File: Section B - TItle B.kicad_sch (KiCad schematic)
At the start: 0 parts

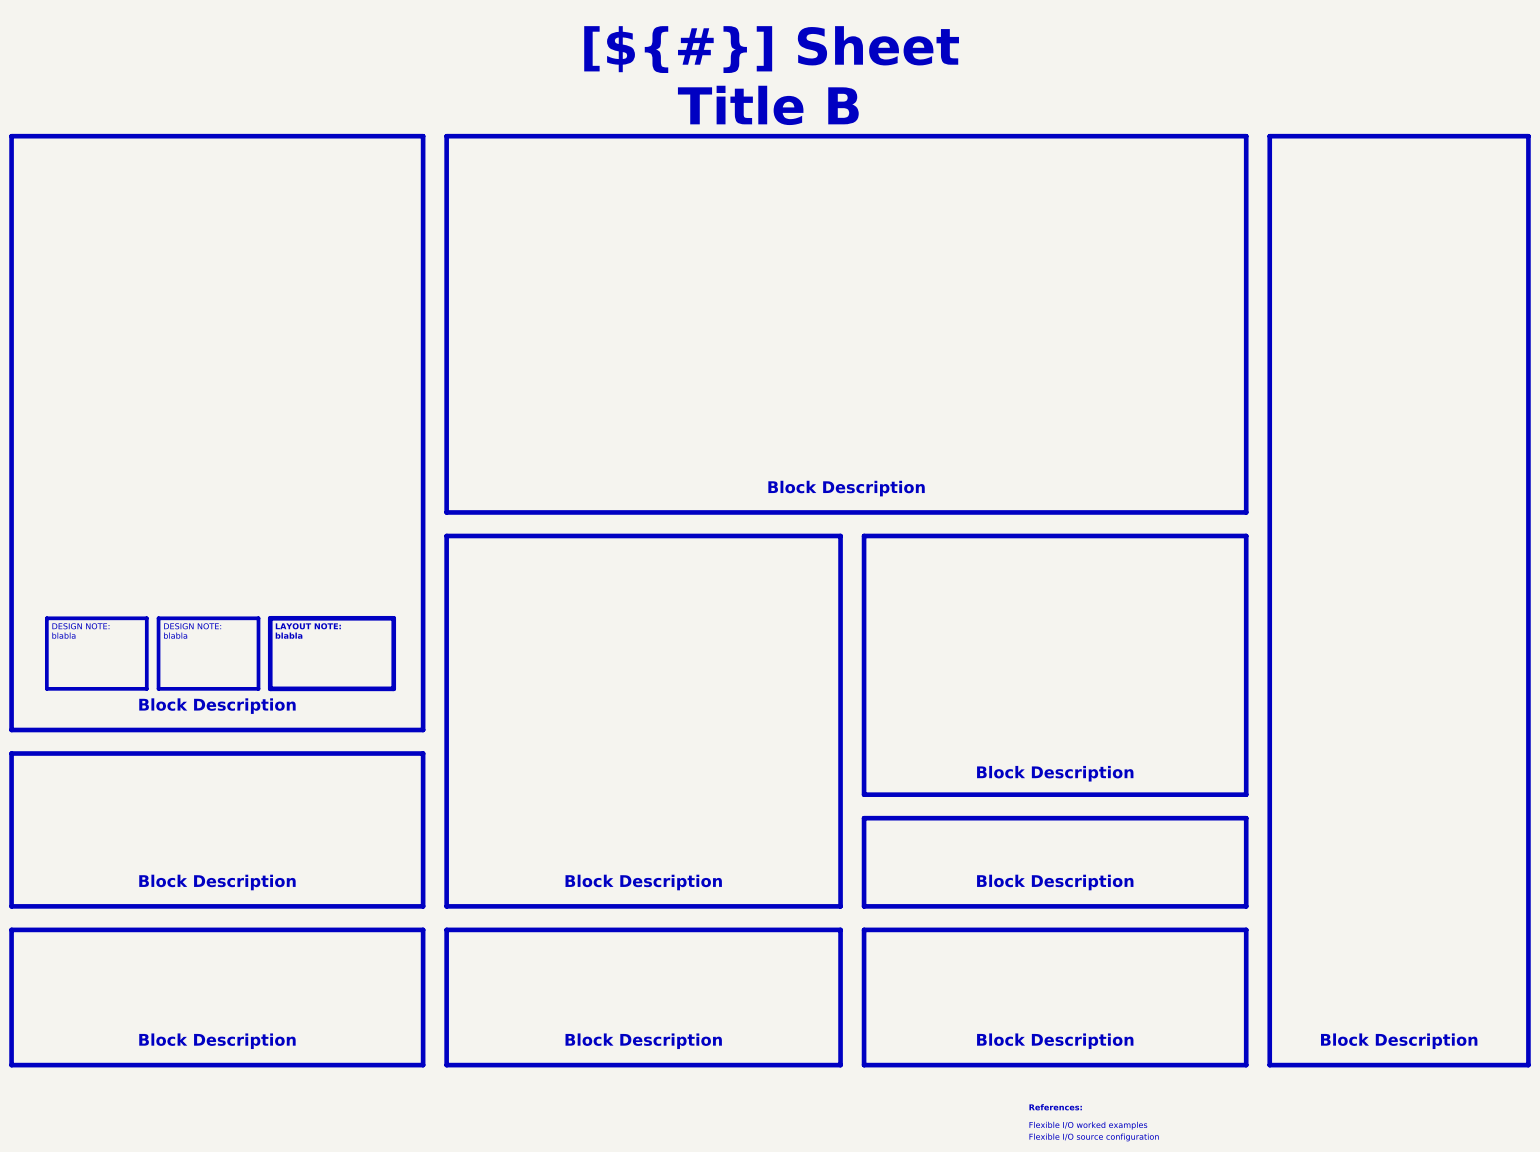
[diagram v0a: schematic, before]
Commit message: feat: Changed templates to be specific to Ryan Dynamics
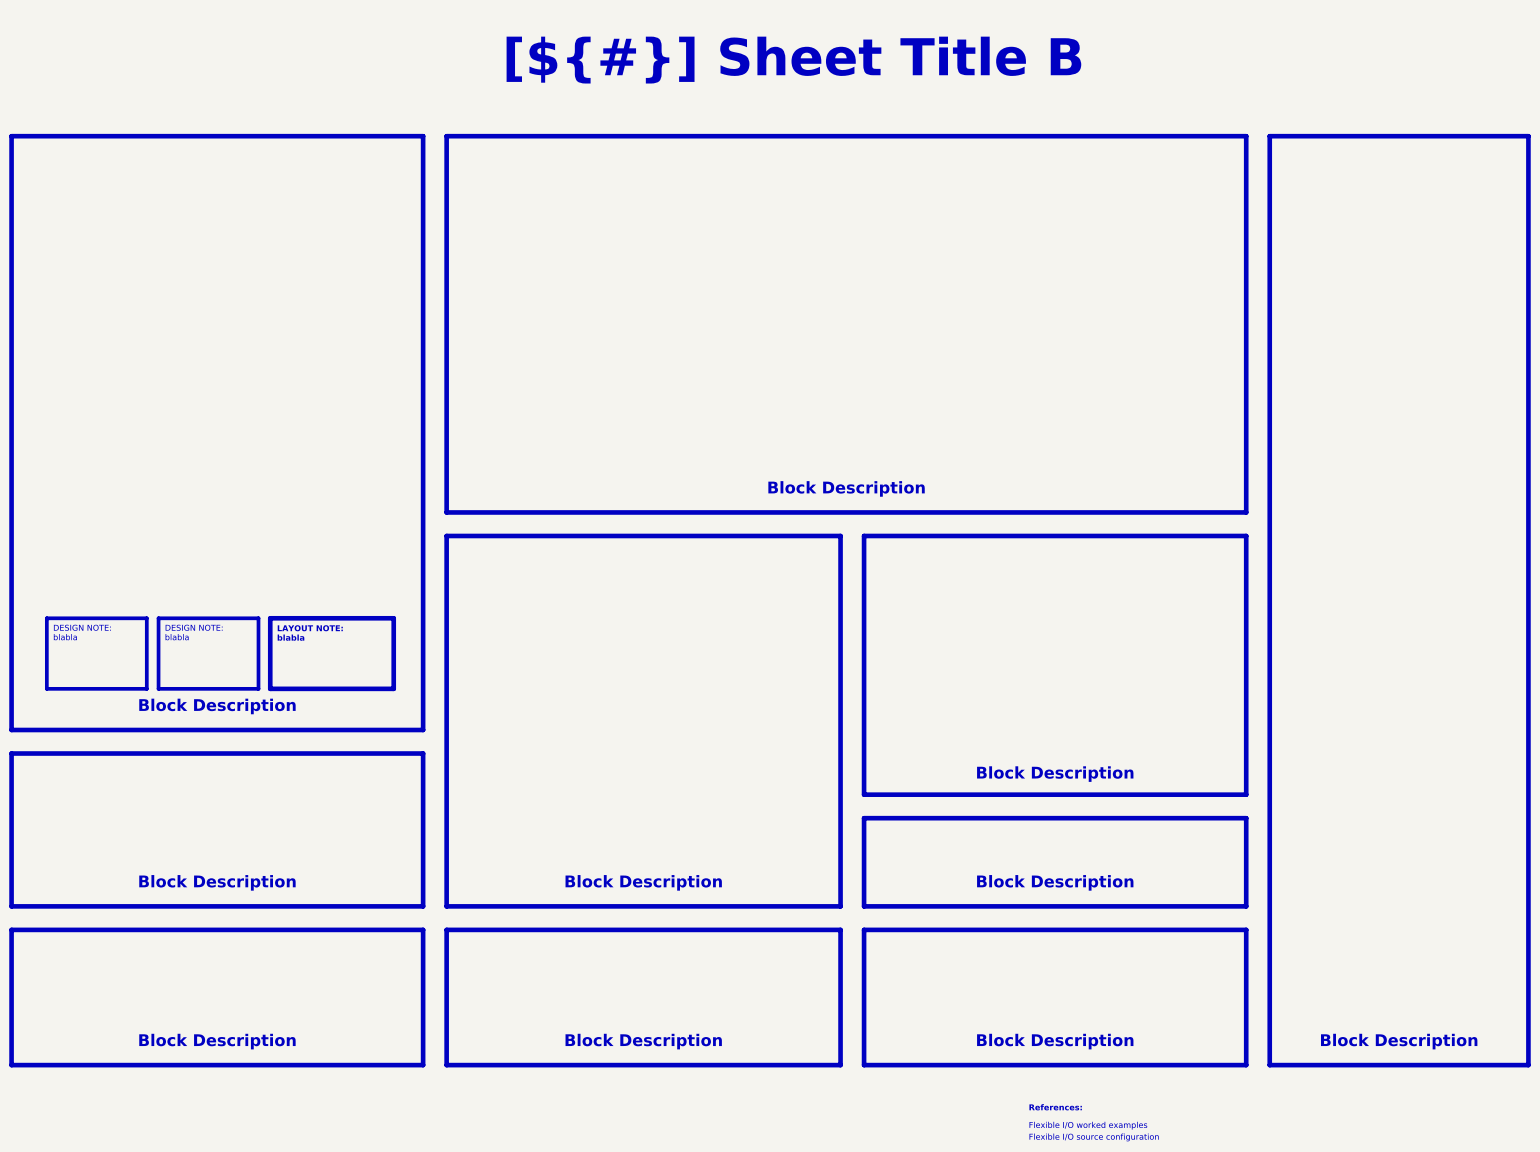
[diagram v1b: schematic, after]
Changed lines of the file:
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@@
 (kicad_sch
-	(version 20231120)
+	(version 20250114)
 	(generator "eeschema")
-	(generator_version "8.0")
+	(generator_version "9.0")
 	(paper "A3")
 	(title_block
@@
 		)
 	)
+	(text "Flexible I/O worked examples"
+		(exclude_from_sim no)
+		(at 265.43 254 0)
+		(effects
+			(font
+				(face "Arial")
+				(size 1.27 1.27)
+				(color 0 0 0 1)
+			)
+			(justify left bottom)
+			(href "https://jpieper.com/2022/06/30/flexible-i-o-worked-examples/")
+		)
+	)
+	(text "References:"
+		(exclude_from_sim no)
+		(at 265.43 250.19 0)
+		(effects
+			(font
+				(face "Arial")
+				(size 1.27 1.27)
+				(thickness 0.254)
+				(bold yes)
+				(color 0 0 0 1)
+			)
+			(justify left bottom)
+		)
+	)
+	(text "Flexible I/O source configuration"
+		(exclude_from_sim no)
+		(at 265.43 256.54 0)
+		(effects
+			(font
+				(face "Arial")
+				(size 1.27 1.27)
+				(color 0 0 0 1)
+			)
+			(justify left bottom)
+			(href "https://jpieper.com/2022/06/28/flexible-i-o-source-configuration/")
+		)
+	)
 	(text_box "Block Description"
 		(exclude_from_sim no)
 		(at 46.99 194.31 0)
 		(size 86.36 9.525)
-		(stroke
-			(width -0.0001)
-			(type default)
-		)
-		(fill
-			(type none)
-		)
-		(effects
-			(font
-				(face "Times New Roman")
+		(margins 1.9049 1.9049 1.9049 1.9049)
+		(stroke
+			(width -0.0001)
+			(type default)
+		)
+		(fill
+			(type none)
+		)
+		(effects
+			(font
 				(size 2.54 2.54)
 				(thickness 0.508)
@@
 		(at 140.97 228.6 0)
 		(size 82.55 9.525)
-		(stroke
-			(width -0.0001)
-			(type default)
-		)
-		(fill
-			(type none)
-		)
-		(effects
-			(font
-				(face "Times New Roman")
+		(margins 1.9049 1.9049 1.9049 1.9049)
+		(stroke
+			(width -0.0001)
+			(type default)
+		)
+		(fill
+			(type none)
+		)
+		(effects
+			(font
 				(size 2.54 2.54)
 				(thickness 0.508)
@@
 	(text_box "[${#}] ${TITLE}"
 		(exclude_from_sim no)
-		(at 161.29 20.32 0)
-		(size 96.52 12.7)
-		(stroke
-			(width -0.0001)
-			(type default)
-		)
-		(fill
-			(type none)
-		)
-		(effects
-			(font
-				(face "Times New Roman")
+		(at 140.97 15 0)
+		(size 147.32 15)
+		(margins 5.9999 5.9999 5.9999 5.9999)
+		(stroke
+			(width -0.0001)
+			(type default)
+		)
+		(fill
+			(type none)
+		)
+		(effects
+			(font
 				(size 8 8)
 				(thickness 1.2)
@@
 		(at 46.99 228.6 0)
 		(size 86.36 9.525)
-		(stroke
-			(width -0.0001)
-			(type default)
-		)
-		(fill
-			(type none)
-		)
-		(effects
-			(font
-				(face "Times New Roman")
+		(margins 1.9049 1.9049 1.9049 1.9049)
+		(stroke
+			(width -0.0001)
+			(type default)
+		)
+		(fill
+			(type none)
+		)
+		(effects
+			(font
 				(size 2.54 2.54)
 				(thickness 0.508)
@@
 		(at 77.47 143.51 0)
 		(size 21.59 15.24)
+		(margins 1.3525 1.3525 1.3525 1.3525)
 		(stroke
 			(width 0.8)
@@
 		(at 231.14 228.6 0)
 		(size 80.01 9.525)
-		(stroke
-			(width -0.0001)
-			(type default)
-		)
-		(fill
-			(type none)
-		)
-		(effects
-			(font
-				(face "Times New Roman")
+		(margins 1.9049 1.9049 1.9049 1.9049)
+		(stroke
+			(width -0.0001)
+			(type default)
+		)
+		(fill
+			(type none)
+		)
+		(effects
+			(font
 				(size 2.54 2.54)
 				(thickness 0.508)
@@
 		(at 101.6 143.51 0)
 		(size 26.67 15.24)
+		(margins 1.4525 1.4525 1.4525 1.4525)
 		(stroke
 			(width 1)
@@
 		(at 46.99 156.21 0)
 		(size 86.36 9.525)
-		(stroke
-			(width -0.0001)
-			(type default)
-		)
-		(fill
-			(type none)
-		)
-		(effects
-			(font
-				(face "Times New Roman")
+		(margins 1.9049 1.9049 1.9049 1.9049)
+		(stroke
+			(width -0.0001)
+			(type default)
+		)
+		(fill
+			(type none)
+		)
+		(effects
+			(font
 				(size 2.54 2.54)
 				(thickness 0.508)
@@
 		(at 142.24 109.22 0)
 		(size 167.64 9.525)
-		(stroke
-			(width -0.0001)
-			(type default)
-		)
-		(fill
-			(type none)
-		)
-		(effects
-			(font
-				(face "Times New Roman")
+		(margins 1.9049 1.9049 1.9049 1.9049)
+		(stroke
+			(width -0.0001)
+			(type default)
+		)
+		(fill
+			(type none)
+		)
+		(effects
+			(font
 				(size 2.54 2.54)
 				(thickness 0.508)
@@
 		(at 231.775 170.815 0)
 		(size 78.74 9.525)
-		(stroke
-			(width -0.0001)
-			(type default)
-		)
-		(fill
-			(type none)
-		)
-		(effects
-			(font
-				(face "Times New Roman")
+		(margins 1.9049 1.9049 1.9049 1.9049)
+		(stroke
+			(width -0.0001)
+			(type default)
+		)
+		(fill
+			(type none)
+		)
+		(effects
+			(font
 				(size 2.54 2.54)
 				(thickness 0.508)
@@
 		(at 231.14 194.31 0)
 		(size 80.01 9.525)
-		(stroke
-			(width -0.0001)
-			(type default)
-		)
-		(fill
-			(type none)
-		)
-		(effects
-			(font
-				(face "Times New Roman")
+		(margins 1.9049 1.9049 1.9049 1.9049)
+		(stroke
+			(width -0.0001)
+			(type default)
+		)
+		(fill
+			(type none)
+		)
+		(effects
+			(font
 				(size 2.54 2.54)
 				(thickness 0.508)
@@
 		(at 318.77 228.6 0)
 		(size 53.34 9.525)
+		(margins 1.9049 1.9049 1.9049 1.9049)
 		(stroke
 			(width -0.0001)
@@
 		(at 53.34 143.51 0)
 		(size 21.59 15.24)
+		(margins 1.3525 1.3525 1.3525 1.3525)
 		(stroke
 			(width 0.8)
@@
 		(at 140.97 194.31 0)
 		(size 82.55 9.525)
-		(stroke
-			(width -0.0001)
-			(type default)
-		)
-		(fill
-			(type none)
-		)
-		(effects
-			(font
-				(face "Times New Roman")
-				(size 2.54 2.54)
-				(thickness 0.508)
-				(bold yes)
-				(color 162 22 34 1)
-			)
-			(justify bottom)
-		)
-	)
-	(text "Flexible I/O worked examples"
-		(exclude_from_sim no)
-		(at 265.43 254 0)
-		(effects
-			(font
-				(face "Arial")
-				(size 1.27 1.27)
-				(color 0 0 0 1)
-			)
-			(justify left bottom)
-			(href "https://jpieper.com/2022/06/30/flexible-i-o-worked-examples/")
-		)
-	)
-	(text "References:"
-		(exclude_from_sim no)
-		(at 265.43 250.19 0)
-		(effects
-			(font
-				(face "Arial")
-				(size 1.27 1.27)
-				(thickness 0.254)
-				(bold yes)
-				(color 0 0 0 1)
-			)
-			(justify left bottom)
-		)
-	)
-	(text "Flexible I/O source configuration"
-		(exclude_from_sim no)
-		(at 265.43 256.54 0)
-		(effects
-			(font
-				(face "Arial")
-				(size 1.27 1.27)
-				(color 0 0 0 1)
-			)
-			(justify left bottom)
-			(href "https://jpieper.com/2022/06/28/flexible-i-o-source-configuration/")
-		)
-	)
+		(margins 1.9049 1.9049 1.9049 1.9049)
+		(stroke
+			(width -0.0001)
+			(type default)
+		)
+		(fill
+			(type none)
+		)
+		(effects
+			(font
+				(size 2.54 2.54)
+				(thickness 0.508)
+				(bold yes)
+				(color 162 22 34 1)
+			)
+			(justify bottom)
+		)
+	)
